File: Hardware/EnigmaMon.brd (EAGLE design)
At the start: 100 x 80 mm, 56 parts, among them IC1 4051N, IC2 TLC5940, T1 BC548, T2 BC548, T3 BC548, T4 BC548, T5 BC548, T6 BC548, T8 BC548, T9 BC548

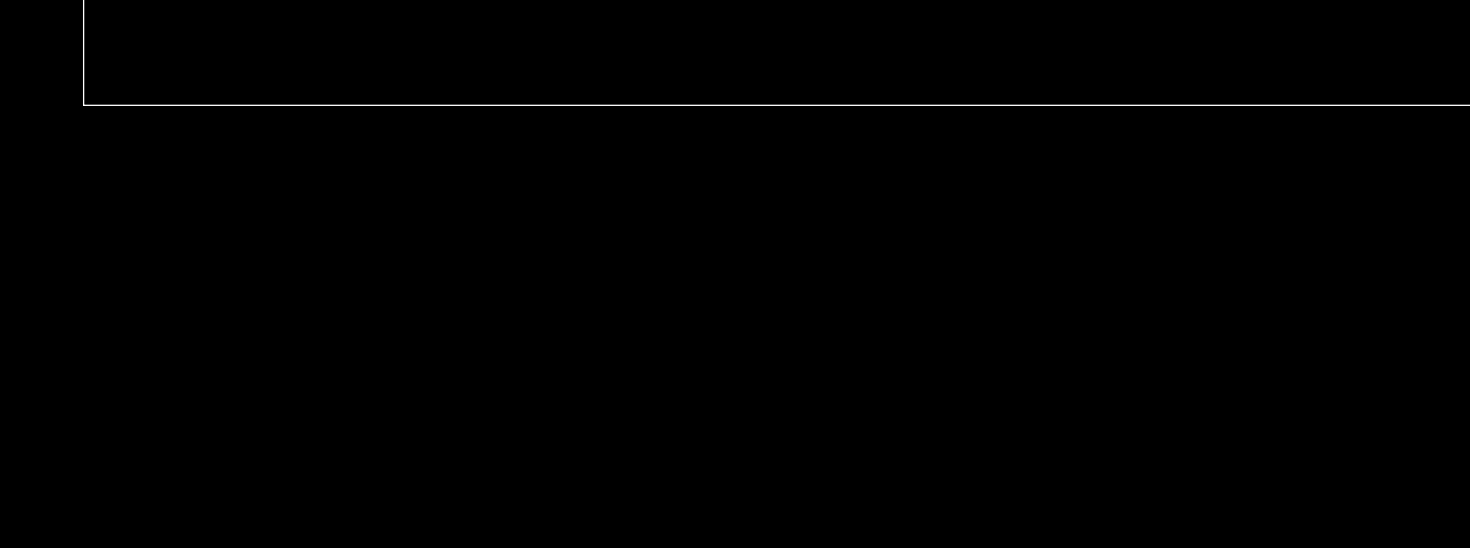
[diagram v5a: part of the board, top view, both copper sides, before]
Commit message: Added some test schematics
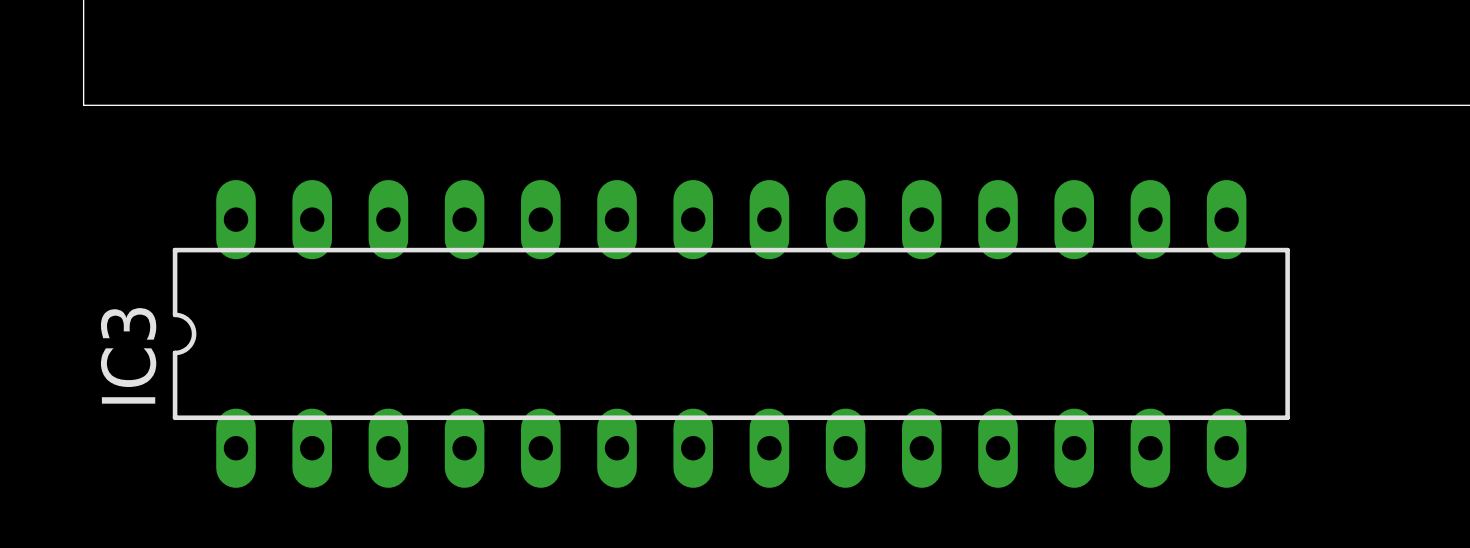
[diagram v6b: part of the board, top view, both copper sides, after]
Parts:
- added IC3: MEGA8-P, EnigmaMon:DIL28-3
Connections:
- new net AVCC: IC3.20
- new net IO0: IC3.2
- new net IO1: IC3.3
- new net IO2: IC3.4
- new net IO3: IC3.5
- new net IO4: IC3.6
- new net IO5: IC3.11
- new net IO6: IC3.12
- new net IO7: IC3.13
- new net IO8: IC3.14
- new net IO9: IC3.15
- net GND: now also IC3.22, IC3.8
- net RESET: now also IC3.1
- net VCC: now also IC3.7
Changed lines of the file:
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@@
 <element name="R14" library="rcl" package="0204/7" value="220" x="8.89" y="76.2"/>
 <element name="RST" library="EnigmaMon" package="DTS6" value="DTS6" x="6.35" y="53.34" rot="R90"/>
+<element name="IC3" library="EnigmaMon" package="DIL28-3" value="MEGA8-P" x="21.59" y="-7.62">
+<attribute name="OC_NEWARK" value="unknown" x="21.59" y="-7.62" size="1.778" layer="27" display="off"/>
+<attribute name="MPN" value="" x="21.59" y="-7.62" size="1.778" layer="27" display="off"/>
+<attribute name="MF" value="" x="21.59" y="-7.62" size="1.778" layer="27" display="off"/>
+<attribute name="OC_FARNELL" value="unknown" x="21.59" y="-7.62" size="1.778" layer="27" display="off"/>
+</element>
 </elements>
 <signals>
@@
 <wire x1="54.61" y1="22.86" x2="57.15" y2="22.86" width="0.8128" layer="16"/>
 <wire x1="44.45" y1="22.86" x2="44.45" y2="15.24" width="0.8128" layer="16"/>
+<contactref element="IC3" pad="22"/>
+<contactref element="IC3" pad="8"/>
+<wire x1="20.32" y1="-3.81" x2="44.45" y2="15.24" width="0" layer="19" extent="1-1"/>
+<wire x1="22.86" y1="-11.43" x2="20.32" y2="-3.81" width="0" layer="19" extent="1-1"/>
 </signal>
 <signal name="FAN4_TACHO">
@@
 <contactref element="R14" pad="2"/>
 <wire x1="12.7" y1="76.2" x2="12.7" y2="68.58" width="0.8128" layer="16"/>
-<wire x1="12.7" y1="68.58" x2="8.89" y2="68.58" width="0" layer="19" extent="1-16"/>
+<contactref element="IC3" pad="7"/>
+<wire x1="20.32" y1="-11.43" x2="54.61" y2="4.33605" width="0" layer="19" extent="16-16"/>
 </signal>
 <signal name="TACHO_SEL2">
@@
 <wire x1="5.08" y1="73.66" x2="8.89" y2="73.66" width="0.4064" layer="16"/>
 <wire x1="3.81" y1="57.15" x2="3.81" y2="50.8" width="0.4064" layer="16"/>
+<contactref element="IC3" pad="1"/>
+<wire x1="5.08" y1="-11.43" x2="3.81" y2="50.8" width="0" layer="19" extent="1-1"/>
+</signal>
+<signal name="AVCC">
+<contactref element="IC3" pad="20"/>
+</signal>
+<signal name="IO0">
+<contactref element="IC3" pad="2"/>
+</signal>
+<signal name="IO1">
+<contactref element="IC3" pad="3"/>
+</signal>
+<signal name="IO2">
+<contactref element="IC3" pad="4"/>
+</signal>
+<signal name="IO3">
+<contactref element="IC3" pad="5"/>
+</signal>
+<signal name="IO4">
+<contactref element="IC3" pad="6"/>
+</signal>
+<signal name="IO5">
+<contactref element="IC3" pad="11"/>
+</signal>
+<signal name="IO6">
+<contactref element="IC3" pad="12"/>
+</signal>
+<signal name="IO7">
+<contactref element="IC3" pad="13"/>
+</signal>
+<signal name="IO8">
+<contactref element="IC3" pad="14"/>
+</signal>
+<signal name="IO9">
+<contactref element="IC3" pad="15"/>
 </signal>
 </signals>

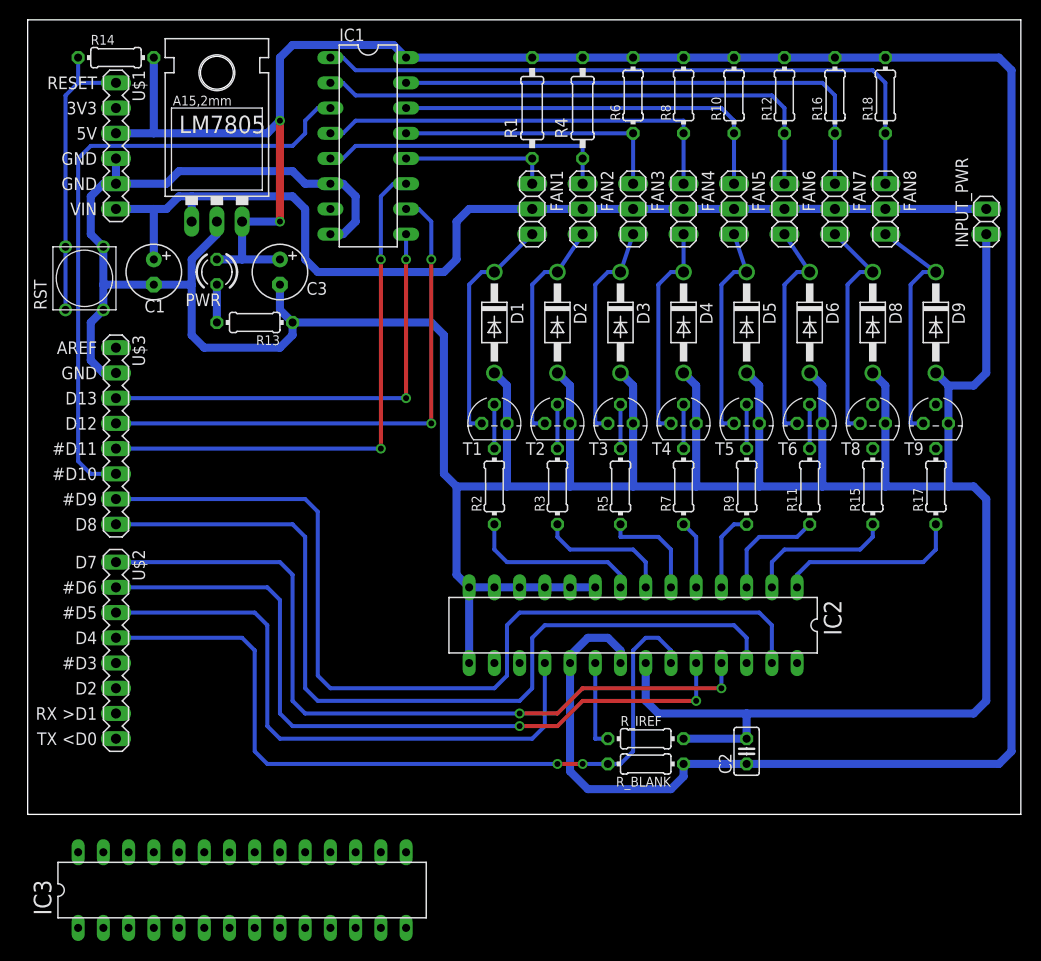
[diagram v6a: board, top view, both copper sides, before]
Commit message: Started wiring for on-board ATmega
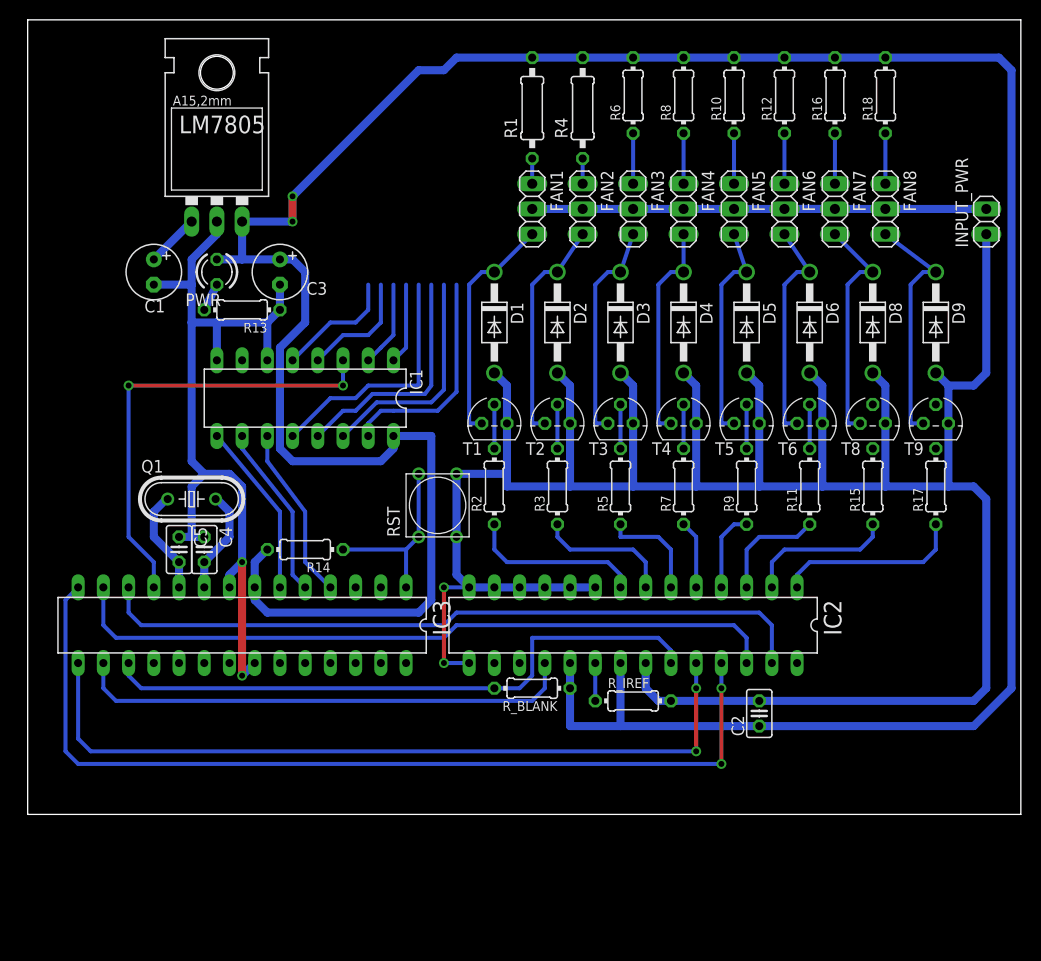
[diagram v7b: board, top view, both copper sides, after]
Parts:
- removed U$1: ARD_POWER, EnigmaMon:ARD_POWER
- removed U$2: ARD_DIGITAL_1, EnigmaMon:ARD_DIGITAL_1
- removed U$3: ARD_DIGITAL_2, EnigmaMon:ARD_DIGITAL_2
- added C4, C5: 10uF, rcl:C025-025X050
- added Q1: (no value), EnigmaMon:HC49/S
- moved R14 53.1 mm to (27.9, 26.7), turned to 180 degrees
- moved RST 42.3 mm to (41.9, 30.5)
- moved IC3 26.7 mm to (21.6, 19.1), turned to 180 degrees
- moved IC1 26.2 mm to (27.9, 41.9), turned to 180 degrees
- moved R_BLANK 13.7 mm to (50.8, 12.7)
- moved C2 4.02 mm to (73.7, 10.2)
- moved R_IREF 4.02 mm to (61.0, 11.4)
- moved R13 1.80 mm to (21.6, 50.8)
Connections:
- removed net IO2: IC3.4
- removed net IO3: IC3.5
- removed net IO4: IC3.6
- removed net IO5: IC3.11
- removed net IO6: IC3.12
- removed net IO7: IC3.13
- removed net IO8: IC3.14
- removed net IO9: IC3.15
- new net IO12: IC3.18
- new net IO13: IC3.19
- new net N$11: C4.2, IC3.9, Q1.2
- new net N$12: C5.2, IC3.10, Q1.1
- net +12V: no longer U$1.VIN
- net FAN_TACHO: now also IC3.11; no longer U$3.10
- net GND: now also C4.1, C5.1; no longer U$1.GND@1, U$1.GND@2, U$3.GND
- net PWM_BLANK: now also IC3.17; no longer U$2.4
- net PWM_GSCLK: now also IC3.16; no longer U$2.5
- net PWM_SCLK: now also IC3.14; no longer U$2.7
- net PWM_SIN: now also IC3.13; no longer U$3.8
- net PWM_VPRG: now also IC3.12; no longer U$3.9
- net PWM_XLAT: now also IC3.15; no longer U$2.6
- net RESET: no longer U$1.RESET
- net TACHO_SEL0: now also IC3.4; no longer U$3.11
- net TACHO_SEL1: now also IC3.5; no longer U$3.12
- net TACHO_SEL2: now also IC3.6; no longer U$3.13
- net VCC: no longer U$1.5V
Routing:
- net +12V: track 111.9 -> 56.2 mm
- net FAN8_TACHO: track 67.1 -> 13.2 mm
- net GND: track 394.5 -> 350.1 mm, vias 0 -> 4
- net FAN6_TACHO: track 54.4 -> 13.8 mm
- net TACHO_SEL1: track 55.1 -> 17.5 mm, vias 2 -> 0
- net TACHO_SEL0: track 55.1 -> 17.6 mm, vias 2 -> 0
- net VCC: track 265.7 -> 297.8 mm
- net TACHO_SEL2: track 45.7 -> 17.5 mm, vias 2 -> 0
- net FAN4_TACHO: track 42.4 -> 16.8 mm
- net FAN7_TACHO: track 52.6 -> 27.4 mm
- net PWM_VPRG: track 94.1 -> 72.7 mm
- net FAN_TACHO: track 63.1 -> 45.5 mm, vias 0 -> 2
- net PWM_BLANK: track 80.1 -> 62.5 mm
- net PWM_SIN: track 89.0 -> 72.7 mm
- net PWM_SCLK: track 78.3 -> 93.8 mm
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
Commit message: Testing
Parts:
- D1, D2, D3, D4, D5, D6, D8, D9: value 1N4004 -> (none); device diode:DO41-10 -> diode:D-5
- FAN1, FAN2, FAN3, FAN4, FAN5, FAN6, FAN7, FAN8: value (none) -> FAN; device pinhead:1X03 -> EnigmaMon:FAN_HEADER
- R1, R4: device rcl:0207/10 -> rcl:0204/5
- R10, R11, R12, R15, R16, R17, R18, R2, R3, R5, R6, R7, R8, R9: device rcl:0204/7 -> rcl:0204/5
- moved INPUT_PWR 22.9 mm to (96.5, 36.8)
- moved R2 22.2 mm to (38.1, 53.3)
- moved T1 22.2 mm to (38.1, 59.7), turned to 180 degrees
- moved R3 21.7 mm to (45.7, 53.3)
- moved T2 21.7 mm to (45.7, 59.7), turned to 180 degrees
- moved R5 21.3 mm to (53.3, 53.3)
- moved T3 21.3 mm to (53.3, 59.7), turned to 180 degrees
- moved R7 20.9 mm to (61.0, 53.3)
- moved T4 20.9 mm to (61.0, 59.7), turned to 180 degrees
- moved R9 20.7 mm to (68.6, 53.3)
- moved T5 20.7 mm to (68.6, 59.7), turned to 180 degrees
- moved R11 20.5 mm to (76.2, 53.3)
- moved T6 20.5 mm to (76.2, 59.7), turned to 180 degrees
- moved R15 20.4 mm to (83.8, 53.3)
- moved T8 20.4 mm to (83.8, 59.7), turned to 180 degrees
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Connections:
- removed net FAN1_GND: D1.C, FAN1.3, T1.3
- removed net FAN2_GND: D2.C, FAN2.3, T2.3
- removed net FAN3_GND: D3.C, FAN3.3, T3.3
- removed net FAN4_GND: D4.C, FAN4.3, T4.3
- removed net FAN5_GND: D5.C, FAN5.3, T5.3
- removed net FAN6_GND: D6.C, FAN6.3, T6.3
- removed net FAN7_GND: D8.C, FAN7.3, T8.3
- removed net FAN8_GND: D9.C, FAN8.3, T9.3
- new net N$13: D2.A, FAN2.GND, T2.3
- new net N$14: D3.A, FAN3.GND, T3.3
- new net N$15: D4.A, FAN4.GND, T4.3
- new net N$16: D1.A, FAN1.GND, T1.3
- new net N$17: D9.A, FAN8.GND, T9.3
- new net N$19: D8.A, FAN7.GND, T8.3
- new net N$20: D6.A, FAN6.GND, T6.3
- new net N$21: D5.A, FAN5.GND, T5.3
- net +12V: now also D1.C, D2.C, D3.C, D4.C, D5.C, D6.C, D8.C, D9.C, FAN1.VCC, FAN2.VCC, FAN3.VCC, FAN4.VCC, FAN5.VCC, FAN6.VCC, FAN7.VCC, FAN8.VCC; no longer FAN1.2, FAN2.2, FAN3.2, FAN4.2, FAN5.2, FAN6.2, FAN7.2, FAN8.2
- net FAN1_TACHO: now also FAN1.TACHO; no longer FAN1.1
- net FAN2_TACHO: now also FAN2.TACHO; no longer FAN2.1
- net FAN3_TACHO: now also FAN3.TACHO; no longer FAN3.1
- net FAN4_TACHO: now also FAN4.TACHO; no longer FAN4.1
- net FAN5_TACHO: now also FAN5.TACHO; no longer FAN5.1
- net FAN6_TACHO: now also FAN6.TACHO; no longer FAN6.1
- net FAN7_TACHO: now also FAN7.TACHO; no longer FAN7.1
- net FAN8_TACHO: now also FAN8.TACHO; no longer FAN8.1
- net GND: no longer D1.A, D2.A, D3.A, D4.A, D5.A, D6.A, D8.A, D9.A
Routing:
- net +12V: track 56.2 -> 235.3 mm
- net FAN8_TACHO: track 13.2 -> 70.1 mm
- net FAN6_TACHO: track 13.8 -> 53.8 mm
- net FAN7_TACHO: track 27.4 -> 62.0 mm
- net VCC: track 297.8 -> 332.2 mm, vias 2 -> 1
- net FAN1_PWM: track 17.6 -> 49.5 mm
- net FAN2_PWM: track 13.8 -> 44.4 mm
- net GND: track 350.1 -> 319.5 mm
- net FAN3_PWM: track 10.7 -> 39.4 mm
- net FAN4_PWM: track 6.88 -> 34.3 mm
- net FAN8_GND: track 24.7 -> 0.00 mm
- net FAN7_GND: track 23.7 -> 0.00 mm
- net FAN1_GND: track 23.7 -> 0.00 mm
- net FAN8_PWM: track 18.8 -> 41.9 mm
- net FAN2_GND: track 22.9 -> 0.00 mm
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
